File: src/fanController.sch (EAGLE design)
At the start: 18 parts, among them Q1 MOSFET-NCHANNELFDD8780

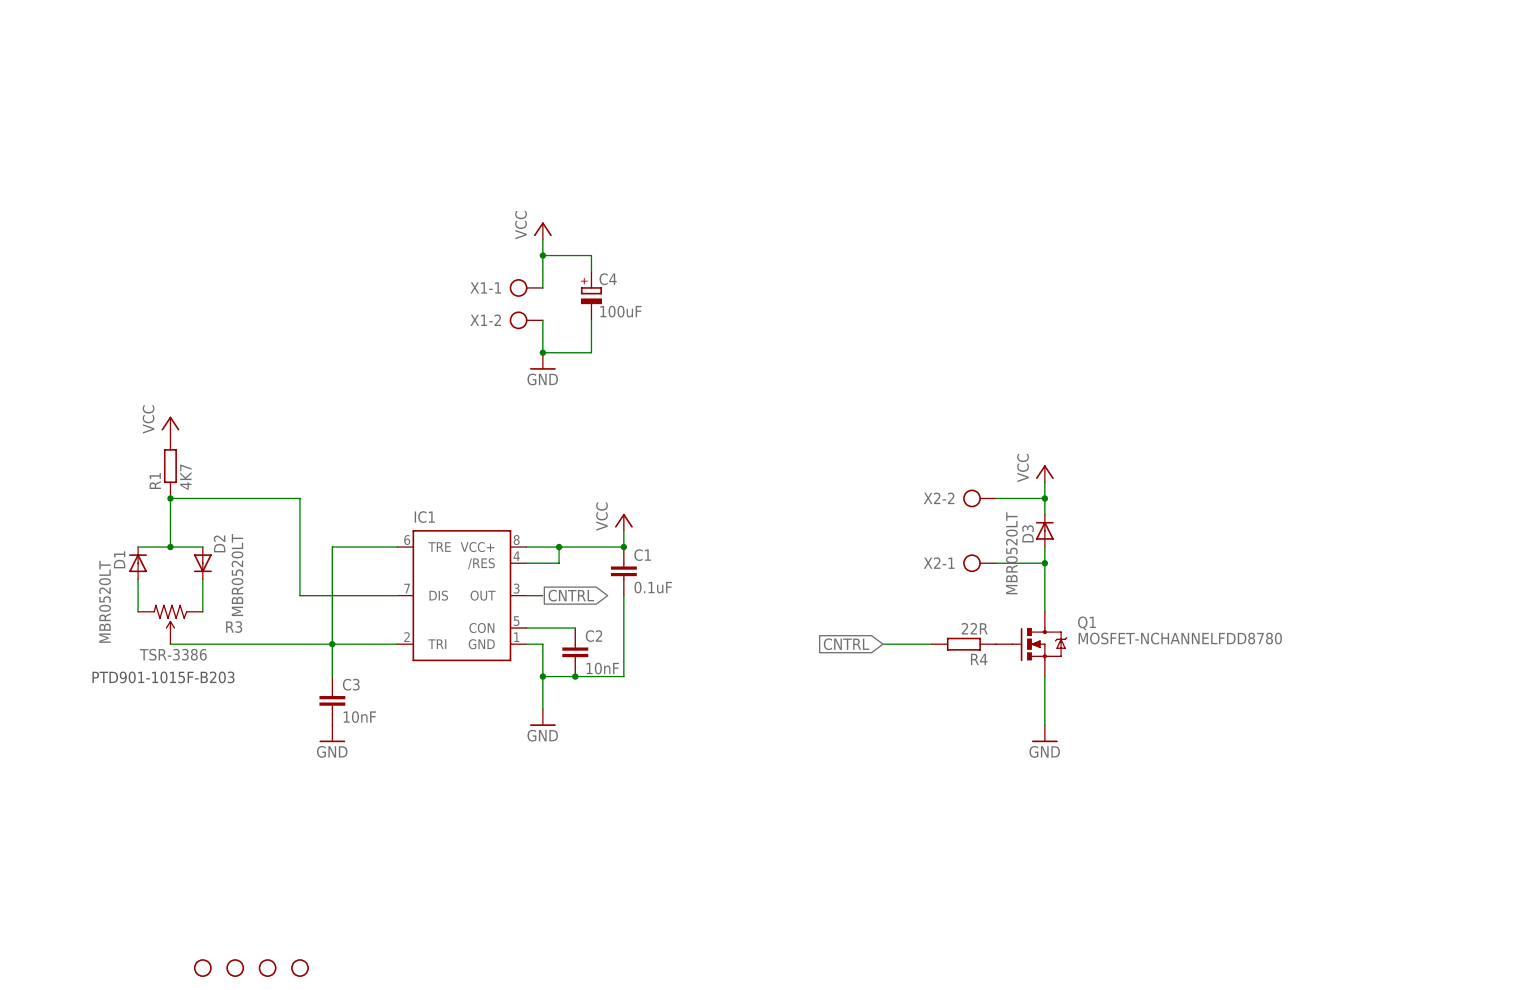
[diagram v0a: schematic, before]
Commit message: Reworked controller for different configuration.
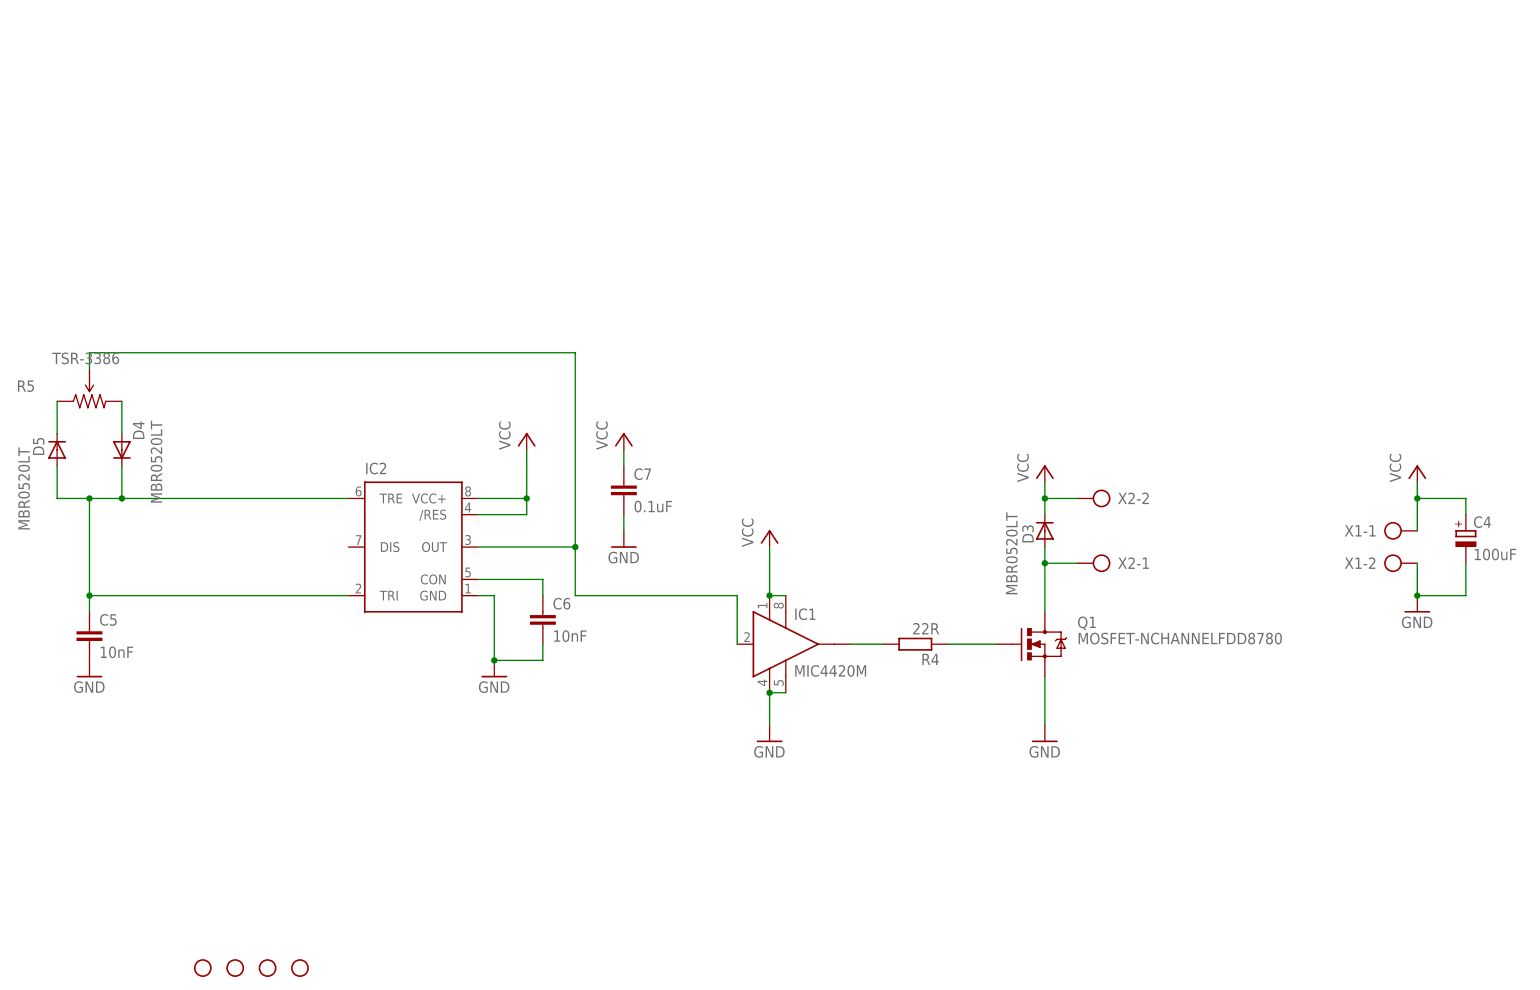
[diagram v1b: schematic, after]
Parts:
- removed C1: 0.1uF, resistor:C-EUC0805
- removed C2, C3: 10nF, resistor:C-EUC0805
- removed D1, D2: MBR0520LT, diode:MBR0520LT
- removed R1: 4K7, resistor:R-EU_M0805
- removed R3: TSR-3386, SparkFun-Electromechanical:TRIMPOT-PTH-KNOB
- added C5, C6: 10nF, resistor:C-EUC0805
- added C7: 0.1uF, resistor:C-EUC0805
- added D4, D5: MBR0520LT, diode:MBR0520LT
- added IC2: (no value), SparkFun-AnalogIC:NE555D
- added R5: TSR-3386, SparkFun-Electromechanical:TRIMPOT-PTH-KNOB
- IC1: value (none) -> MIC4420M; device SparkFun-AnalogIC:NE555D -> transistor-power:MIC4420M
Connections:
- net CNTRL: now also IC1.IN, IC2.OUT, R5.WIPER; no longer IC1.OUT, R4.2
- net GND: now also C5.2, C6.2, C7.2, IC1.GND1, IC2.GND; no longer C1.2, C2.2, C3.2
- net N$1: now also D5.C, R5.CCW; no longer C2.1, IC1.CON
- net N$2: now also D4.A, R5.CW; no longer D1.A, R3.CW
- net N$4: now also C5.1, D4.C, D5.A, IC2.TRE, IC2.TRI; no longer C3.1, IC1.TRE, IC1.TRI, R3.WIPER
- net N$5: now also C6.1, IC2.CON; no longer D1.C, D2.A, IC1.DIS, R1.1
- net N$6: now also IC1.OUT@1, R4.2; no longer D2.C, R3.CCW
- net VCC: now also C7.1, IC1.VS, IC1.VS1, IC2./RES, IC2.VCC+; no longer C1.1, IC1./RES, IC1.VCC+, R1.2
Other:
- note removed: "PTD901-1015F-B203"
- moved on the sheet: C4, R4, X1-1, X1-2, X2-1, X2-2

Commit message: Updated Rev B for production.
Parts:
- added C1, C2: 0.1uF, resistor:C-EUC0805
- IC2: value (none) -> NE555
- R5: value TSR-3386 -> TSR-3386-100K
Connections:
- net GND: now also C1.2, C2.2
- net VCC: now also C1.1, C2.1
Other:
- note added: "DC PWM Controller"
- note added: "Released under the CERN Open Hardware Licence v1.2 http://www.ohwr.org/attachments/2388/cern_ohl_v_1_2.txt Copyright (c) 2017 - by F. Malpartida"
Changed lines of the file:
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@@
 <?xml version="1.0" encoding="utf-8"?>
 <!DOCTYPE eagle SYSTEM "eagle.dtd">
-<eagle version="7.6.0">
+<eagle version="8.1.0">
 <drawing>
 <settings>
@@
 <part name="STANDOFF3" library="SparkFun-Electromechanical" deviceset="STAND-OFF" device="TIGHT" value="STAND-OFFTIGHT"/>
 <part name="STANDOFF4" library="SparkFun-Electromechanical" deviceset="STAND-OFF" device="TIGHT" value="STAND-OFFTIGHT"/>
-<part name="IC2" library="SparkFun-AnalogIC" deviceset="NE555" device="D"/>
+<part name="IC2" library="SparkFun-AnalogIC" deviceset="NE555" device="D" value="NE555"/>
 <part name="P+5" library="supply1" deviceset="VCC" device=""/>
 <part name="GND5" library="supply1" deviceset="GND" device=""/>
-<part name="R5" library="SparkFun-Electromechanical" deviceset="TRIMPOT" device="-PTH-KNOB" value="TSR-3386"/>
+<part name="R5" library="SparkFun-Electromechanical" deviceset="TRIMPOT" device="-PTH-KNOB" value="TSR-3386-100K"/>
 <part name="D4" library="diode" deviceset="MBR0520LT" device=""/>
 <part name="D5" library="diode" deviceset="MBR0520LT" device=""/>
@@
 <part name="P+2" library="supply1" deviceset="VCC" device=""/>
 <part name="GND6" library="supply1" deviceset="GND" device=""/>
+<part name="C1" library="resistor" deviceset="C-EU" device="C0805" value="0.1uF"/>
+<part name="C2" library="resistor" deviceset="C-EU" device="C0805" value="0.1uF"/>
+<part name="GND7" library="supply1" deviceset="GND" device=""/>
 </parts>
 <sheets>
 <sheet>
 <plain>
+<text x="68.58" y="25.4" size="1.778" layer="97">Released under the CERN Open Hardware Licence v1.2
+http://www.ohwr.org/attachments/2388/cern_ohl_v_1_2.txt
+Copyright (c) 2017 - by F. Malpartida </text>
+<text x="93.98" y="160.02" size="5.08" layer="97" ratio="12">DC PWM Controller</text>
 </plain>
 <instances>
@@
 <instance part="R5" gate="R?" x="30.48" y="106.68" smashed="yes">
 <attribute name="NAME" x="19.05" y="108.1786" size="1.778" layer="95"/>
-<attribute name="VALUE" x="24.638" y="112.522" size="1.778" layer="96"/>
+<attribute name="VALUE" x="32.004" y="108.458" size="1.778" layer="96"/>
 </instance>
 <instance part="D4" gate="G$1" x="35.56" y="99.06" smashed="yes" rot="R270">
@@
 <instance part="GND2" gate="1" x="114.3" y="83.82"/>
 <instance part="IC1" gate="G$1" x="139.7" y="68.58"/>
-<instance part="P+2" gate="VCC" x="137.16" y="86.36"/>
+<instance part="P+2" gate="VCC" x="137.16" y="97.79"/>
 <instance part="GND6" gate="1" x="137.16" y="53.34"/>
+<instance part="C1" gate="G$1" x="144.78" y="88.9"/>
+<instance part="C2" gate="G$1" x="154.94" y="88.9"/>
+<instance part="GND7" gate="1" x="144.78" y="81.28"/>
 </instances>
 <busses>
@@
 <pinref part="P+2" gate="VCC" pin="VCC"/>
 <pinref part="IC1" gate="G$1" pin="VS"/>
-<wire x1="137.16" y1="83.82" x2="137.16" y2="76.2" width="0.1524" layer="91"/>
+<wire x1="137.16" y1="95.25" x2="137.16" y2="91.44" width="0.1524" layer="91"/>
 <pinref part="IC1" gate="G$1" pin="VS1"/>
+<wire x1="137.16" y1="91.44" x2="137.16" y2="76.2" width="0.1524" layer="91"/>
 <wire x1="139.7" y1="76.2" x2="137.16" y2="76.2" width="0.1524" layer="91"/>
 <junction x="137.16" y="76.2"/>
+<pinref part="C2" gate="G$1" pin="1"/>
+<pinref part="C1" gate="G$1" pin="1"/>
+<wire x1="154.94" y1="91.44" x2="144.78" y2="91.44" width="0.1524" layer="91"/>
+<wire x1="144.78" y1="91.44" x2="137.16" y2="91.44" width="0.1524" layer="91"/>
+<junction x="144.78" y="91.44"/>
+<junction x="137.16" y="91.44"/>
 </segment>
 </net>
@@
 <wire x1="139.7" y1="60.96" x2="137.16" y2="60.96" width="0.1524" layer="91"/>
 <junction x="137.16" y="60.96"/>
+</segment>
+<segment>
+<pinref part="C1" gate="G$1" pin="2"/>
+<pinref part="GND7" gate="1" pin="GND"/>
+<pinref part="C2" gate="G$1" pin="2"/>
+<wire x1="154.94" y1="83.82" x2="144.78" y2="83.82" width="0.1524" layer="91"/>
+<junction x="144.78" y="83.82"/>
 </segment>
 </net>
@@
 </schematic>
 </drawing>
+<compatibility>
+<note version="6.3" minversion="6.2.2" severity="warning">
+Since Version 6.2.2 text objects can contain more than one line,
+which will not be processed correctly with this version.
+</note>
+</compatibility>
 </eagle>
